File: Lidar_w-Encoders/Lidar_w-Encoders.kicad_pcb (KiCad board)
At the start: 2 copper layers, 67 x 61.5 mm, 15 parts, among them J1 DB15_HighDensity_MountingHoles, J2 DB15_HighDensity_MountingHoles, P1 CONN_01X04, P2 CONN_01X04, P3 CONN_01X04, P4 CONN_01X04, P5 CONN_01X05, P6 CONN_01X04, U1 MCP2551-I/P, U2 Teensy3.6

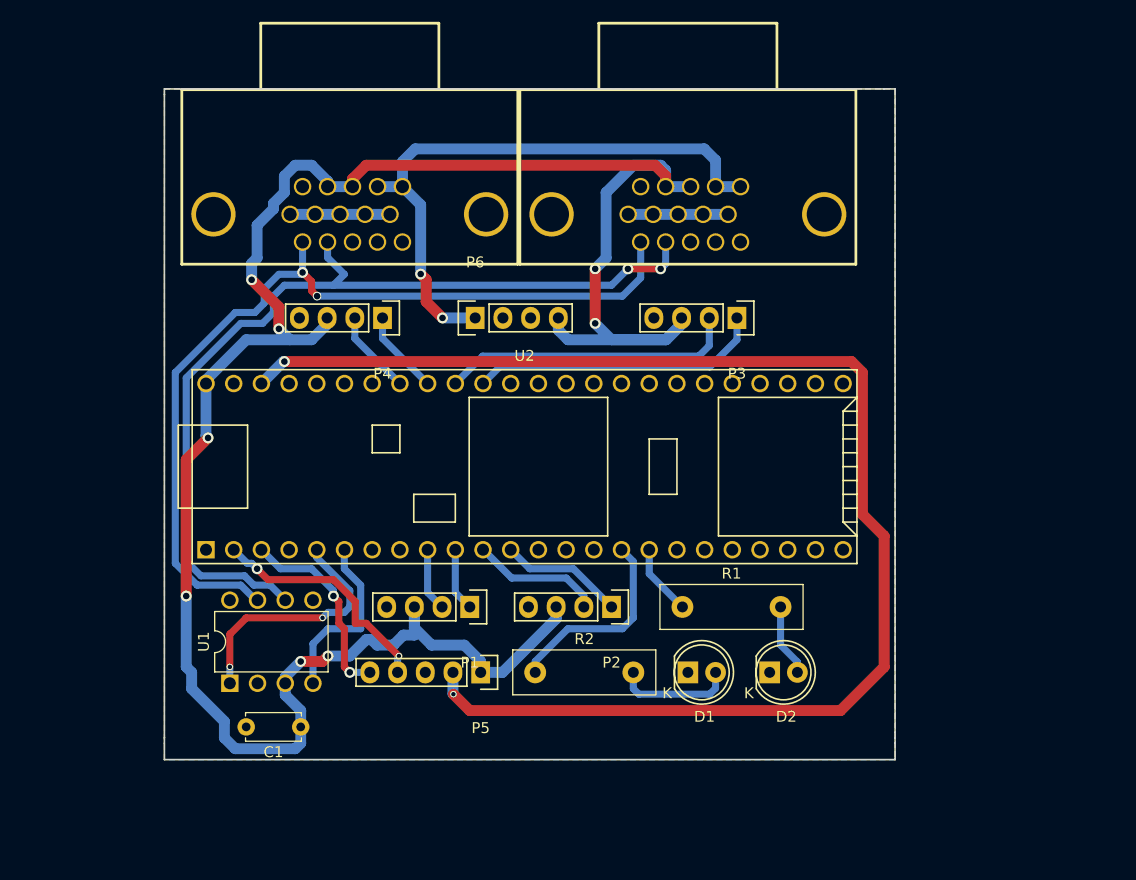
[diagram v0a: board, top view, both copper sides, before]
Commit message: added connector labels and cleaned up
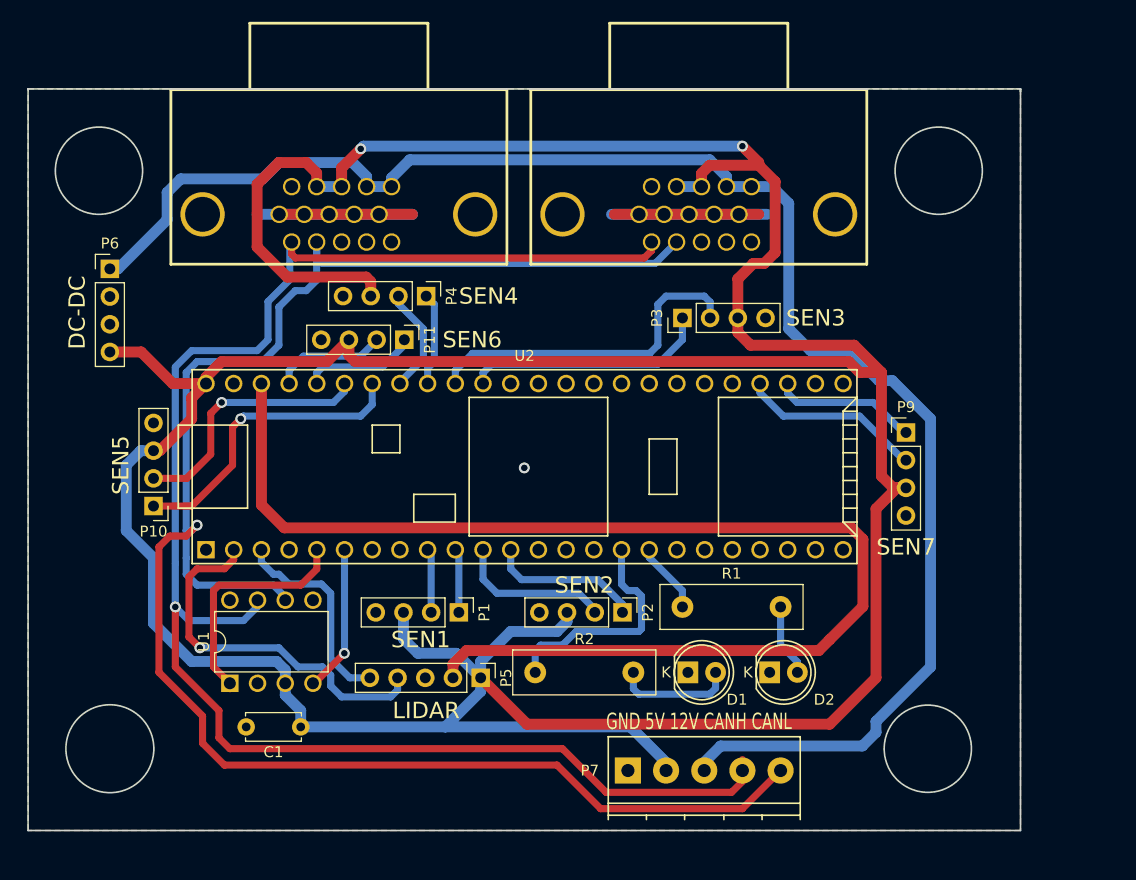
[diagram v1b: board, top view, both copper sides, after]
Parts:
- added P10: CONN_01X04, Socket_Strips:Socket_Strip_Straight_1x04_Pitch2.54mm, F.Cu at (148.0, 119.8)
- added P11: CONN_01X04, Socket_Strips:Socket_Strip_Straight_1x04_Pitch2.54mm, F.Cu at (171.0, 104.5)
- added P7: CONN_01X05, Connectors_Terminal_Blocks:TerminalBlock_Pheonix_PT-3.5mm_5pol, F.Cu at (191.5, 144.0)
- added P9: CONN_01X04, Socket_Strips:Socket_Strip_Straight_1x04_Pitch2.54mm, F.Cu at (217.0, 113.0)
- P1, P2, P3, P4, P6: footprint Socket_Strips:Socket_Strip_Straight_1x04 -> Socket_Strips:Socket_Strip_Straight_1x04_Pitch2.54mm
- P5: footprint Socket_Strips:Socket_Strip_Straight_1x05 -> Socket_Strips:Socket_Strip_Straight_1x05_Pitch2.54mm
- moved P6 33.8 mm to (144.0, 98.0)
- moved P3 5.00 mm to (196.5, 102.5), turned to 90 degrees
- moved P4 4.47 mm to (173.0, 100.5), turned to 270 degrees
- moved P1 1.12 mm to (176.0, 129.5), turned to 270 degrees
- moved P2 1.12 mm to (191.0, 129.5), turned to 270 degrees
- moved J1 1.00 mm to (165.0, 93.0)
- moved J2 1.00 mm to (198.0, 93.0)
- moved P5 0.50 mm to (178.0, 135.5), turned to 270 degrees
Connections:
- U2 pad 32: Net-(U2-Pad32) -> /A7
- U2 pad 33: Net-(U2-Pad33) -> /B7
- U2 pad 47: Net-(U2-Pad47) -> /A5
- U2 pad 48: Net-(U2-Pad48) -> /B5
- U2 pad 49: Net-(U2-Pad49) -> /A6
- U2 pad 50: Net-(U2-Pad50) -> /B6
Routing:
- net +5V: track 203.3 -> 370.7 mm, vias 8 -> 2
- net +12V: track 55.5 -> 149.3 mm, vias 2 -> 0
- net /CANL: track 84.0 -> 167.6 mm, vias 2 -> 1
- net /CANH: track 81.8 -> 152.5 mm, vias 2 -> 1
- net GND: track 18.3 -> 54.0 mm
- net /A5: track 0.00 -> 27.9 mm, vias 0 -> 1
- net /B5: track 0.00 -> 23.7 mm, vias 0 -> 1
- net /B7: track 0.00 -> 16.8 mm
- net /A7: track 0.00 -> 13.2 mm
- net +3V3: track 128.0 -> 114.8 mm, vias 2 -> 0
- net /Tx: track 22.2 -> 34.5 mm, vias 2 -> 1
- net /A6: track 0.00 -> 10.6 mm
- net /B6: track 0.00 -> 10.4 mm
- net /A3: track 26.9 -> 22.5 mm
- net /B3: track 27.4 -> 31.4 mm
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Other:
- board size 67 x 61.5 mm -> 91 x 68 mm
- board text added: "4904 Bot-Provoking"
- board text added: "BP-e-1002"
- board text added: "DC-DC"
- board text added: "GND 5V 12V CANH CANL"
- board text added: "LIDAR"
- board text added: "SEN1"
- board text added: "SEN2"
- board text added: "SEN3"
- board text added: "SEN4"
- board text added: "SEN5"
- board text added: "SEN6"
- board text added: "SEN7"

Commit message: changes
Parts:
- added P8: CONN_01X04, Socket_Strips:Socket_Strip_Straight_1x04_Pitch2.54mm, F.Cu at (218.0, 123.0)
- moved P10 73.0 mm to (218.0, 99.0), turned to 90 degrees
- moved P7 54.6 mm to (142.0, 121.0), turned to 270 degrees
- moved P11 48.6 mm to (218.0, 117.0), turned to 90 degrees
- moved P4 45.2 mm to (218.0, 105.0), turned to 90 degrees
- moved D1 29.1 mm to (226.0, 137.0), turned to 180 degrees
- moved R2 26.1 mm to (209.0, 137.0)
- moved P9 24.8 mm to (199.0, 130.0)
- moved P3 23.1 mm to (218.0, 111.0)
- moved D2 22.1 mm to (226.0, 130.0), turned to 180 degrees
- moved R1 12.5 mm to (209.0, 130.0)
- moved P5 10.3 mm to (170.0, 129.0), turned to 0 degrees
- moved P1 3.04 mm to (179.0, 130.0), turned to 0 degrees
- moved P2 2.06 mm to (189.0, 130.0), turned to 0 degrees
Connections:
- J1 pad 11: Net-(J1-Pad11) -> (no net)
- J1 pad 3: Net-(J1-Pad3) -> (no net)
- J1 pad 4: Net-(J1-Pad4) -> (no net)
- J1 pad 5: Net-(J1-Pad5) -> (no net)
- J2 pad 11: Net-(J2-Pad11) -> (no net)
- J2 pad 3: Net-(J2-Pad3) -> (no net)
- J2 pad 4: Net-(J2-Pad4) -> (no net)
- J2 pad 5: Net-(J2-Pad5) -> (no net)
- P1 pad 1: /B1 -> /A1
- P1 pad 2: /A1 -> /B1
- P10 pad 1: /A5 -> /A6
- P10 pad 2: /B5 -> /B6
- P11 pad 1: /A6 -> /A7
- P11 pad 2: /B6 -> /B7
- P2 pad 1: /B2 -> /A2
- P2 pad 2: /A2 -> /B2
- P3 pad 1: /A3 -> /A4
- P3 pad 2: /B3 -> /B4
- P4 pad 1: /A4 -> /A5
- P4 pad 2: /B4 -> /B5
- P9 pad 1: /A7 -> /A8
- P9 pad 2: /B7 -> /B8
- U1 pad 5: Net-(U1-Pad5) -> (no net)
- U2 pad 13: Net-(U2-Pad13) -> /A8
- U2 pad 14: Net-(U2-Pad14) -> /B8
- U2 pad 15: Net-(U2-Pad15) -> (no net)
- U2 pad 18: Net-(U2-Pad18) -> (no net)
- U2 pad 19: Net-(U2-Pad19) -> (no net)
- U2 pad 20: Net-(U2-Pad20) -> (no net)
- U2 pad 21: Net-(U2-Pad21) -> (no net)
- U2 pad 22: Net-(U2-Pad22) -> (no net)
- U2 pad 23: Net-(U2-Pad23) -> (no net)
- U2 pad 24: Net-(U2-Pad24) -> (no net)
- U2 pad 30: Net-(U2-Pad30) -> (no net)
- U2 pad 31: Net-(U2-Pad31) -> (no net)
- U2 pad 34: Net-(U2-Pad34) -> (no net)
- U2 pad 35: Net-(U2-Pad35) -> (no net)
- U2 pad 36: Net-(U2-Pad36) -> (no net)
- U2 pad 37: Net-(U2-Pad37) -> (no net)
- U2 pad 38: Net-(U2-Pad38) -> (no net)
- U2 pad 4: Net-(U2-Pad4) -> (no net)
- U2 pad 40: Net-(U2-Pad40) -> (no net)
- U2 pad 41: Net-(U2-Pad41) -> (no net)
- U2 pad 42: Net-(U2-Pad42) -> (no net)
- U2 pad 52: Net-(U2-Pad52) -> (no net)
- U2 pad 7: Net-(U2-Pad7) -> (no net)
- U2 pad 8: Net-(U2-Pad8) -> (no net)
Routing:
- net +5V: track 370.7 -> 251.8 mm, vias 2 -> 1
- net /CANL: track 167.6 -> 107.8 mm, vias 1 -> 0
- net /B6: track 10.4 -> 67.7 mm
- net /CANH: track 152.5 -> 95.4 mm, vias 1 -> 0
- net /A6: track 10.6 -> 59.8 mm
- net /B4: track 10.1 -> 54.9 mm
- net +12V: track 149.3 -> 108.0 mm
- net /A4: track 8.58 -> 48.4 mm
- net +3V3: track 114.8 -> 76.3 mm
- net /B5: track 23.7 -> 60.2 mm, vias 1 -> 0
- net /A5: track 27.9 -> 52.3 mm, vias 1 -> 0
- net /A3: track 22.5 -> 45.8 mm
- net /B3: track 31.4 -> 51.8 mm
- net /A8: track 0.00 -> 18.3 mm
- net /B8: track 0.00 -> 16.9 mm
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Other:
- board size 91 x 68 mm -> 100 x 70 mm
- board text added: "BP-E-1002-01"
- board text added: "ERR"
- board text added: "PWR"
- board text added: "SEN8"
- board text removed: "BP-e-1002"
